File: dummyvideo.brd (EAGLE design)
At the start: 26.3 x 27.9 mm, 12 parts, among them IC1 NE555

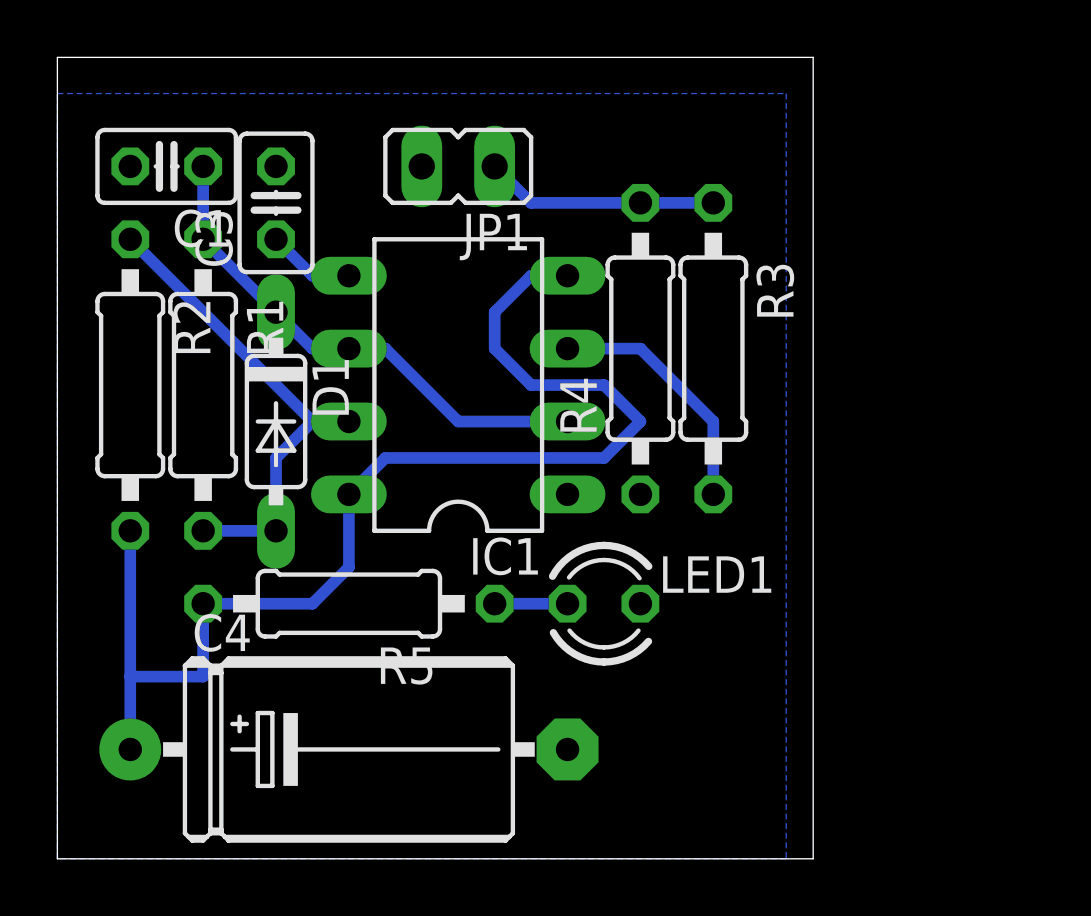
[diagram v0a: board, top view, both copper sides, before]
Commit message: Added power and mount holes.
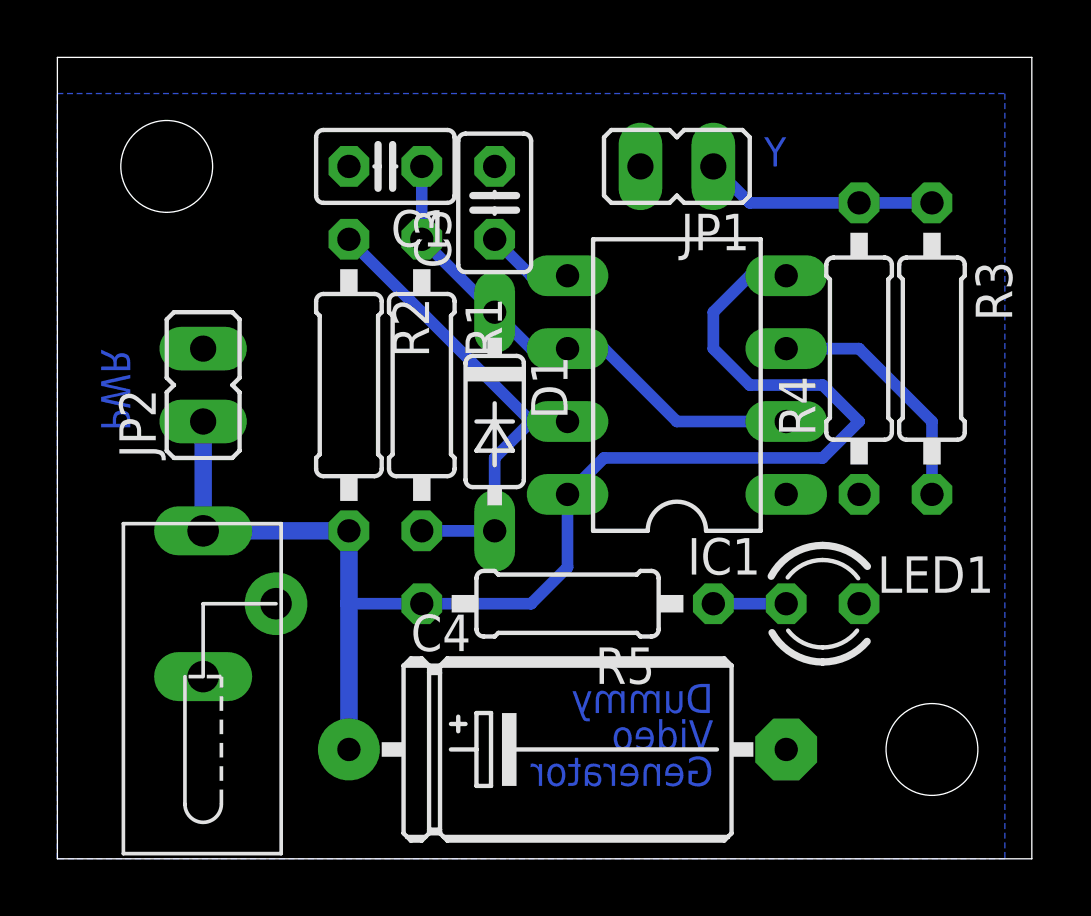
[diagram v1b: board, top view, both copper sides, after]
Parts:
- added JP2: POWER, jumper:JP1
- added U$1: DC_JACK, n39:DC_JACK_HEBO13
- JP1: value (none) -> Y
- moved C4 7.62 mm to (17.8, 3.81)
- moved LED1 7.62 mm to (26.7, 8.89)
- moved R3 7.62 mm to (30.5, 17.8)
- moved R4 7.62 mm to (27.9, 17.8)
- moved R5 7.62 mm to (17.8, 8.89)
- moved C3 7.62 mm to (15.2, 22.9)
- moved D1 7.62 mm to (15.2, 15.2)
- moved R2 7.62 mm to (10.2, 16.5)
- moved C1 7.62 mm to (11.4, 24.1)
- moved IC1 7.62 mm to (21.6, 16.5)
- moved JP1 7.62 mm to (21.6, 24.1)
- moved R1 7.62 mm to (12.7, 16.5)
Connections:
- net GND: now also JP2.2, U$1.OUTER
- net VCC: now also JP2.1, U$1.INNER
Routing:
- net VCC: track 42.5 -> 48.9 mm
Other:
- board size 26.3 x 27.9 mm -> 34 x 27.9 mm
- board text added: "Dummy"
- board text added: "Generator"
- board text added: "PWR"
- board text added: "Video"
- board text added: "Y"

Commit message: Wiederstand vor der LED angepasst
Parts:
- R5: value 220R -> 330R
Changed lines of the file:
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@@
 <element name="R4" library="resistor" package="0207/10" value="1,5K" x="27.94" y="17.78" rot="R90"/>
 <element name="LED1" library="led" package="LED3MM" value="bl" x="26.67" y="8.89"/>
-<element name="R5" library="resistor" package="0207/10" value="220R" x="17.78" y="8.89" rot="R180"/>
+<element name="R5" library="resistor" package="0207/10" value="330R" x="17.78" y="8.89" rot="R180"/>
 <element name="JP1" library="jumper" package="JP1" value="Y" x="21.59" y="24.13" rot="R90"/>
 <element name="U$1" library="n39" package="DC_JACK_HEBO13" value="DC_JACK" x="5.08" y="10.16"/>

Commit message: First revision of SMD board
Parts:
- removed JP1: Y, jumper:JP1
- removed JP2: POWER, jumper:JP1
- removed U$1: DC_JACK, n39:DC_JACK_HEBO13
- added JP_PAD1, JP_PAD2, PAD_Y, PWR_PAD_GND, PWR_PAD_VCC: (no value), wirepad:SMD1,27-2,54
- C1, C3: device resistor:C025-025X050 -> resistor:C0805
- C4: value 100u -> 47u; device resistor:E15-6 -> resistor:153CLV-0505
- IC1: value NE555 -> NE555SO; device st-microelectronics:DIL-08 -> n39:SO08
- LED1: value bl -> gn LC; device led:LED3MM -> led:CHIPLED-0603-TTW
- R1, R3, R4: device resistor:0207/10 -> resistor:R0805
- R2: device resistor:0207/10 -> resistor:M0805
- R5: value 330R -> 1,5K; device resistor:0207/10 -> resistor:R0805
- moved LED1 70.1 mm to (-33.0, 45.7)
- moved R4 63.5 mm to (-31.8, 39.4), turned to 0 degrees
- moved R3 54.0 mm to (-19.1, 39.4), turned to 0 degrees
- moved R5 51.2 mm to (-19.1, 44.5), turned to 0 degrees
- moved C1 48.4 mm to (-36.8, 20.3), turned to 0 degrees
- moved D1 46.6 mm to (-29.2, 29.2), turned to 0 degrees
- moved R2 45.5 mm to (-31.8, 34.3), turned to 0 degrees
- moved C4 42.7 mm to (-21.6, 20.3)
- moved R1 36.4 mm to (-19.1, 34.3), turned to 0 degrees
- moved C3 31.1 mm to (-15.2, 29.2), turned to 0 degrees
- moved IC1 13.0 mm to (8.89, 19.1), turned to 0 degrees
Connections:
- new net N$6: JP_PAD2.1, PWR_PAD_VCC.1
- net GND: now also LED1.C@1, PWR_PAD_GND.1; no longer JP1.2, JP2.2, LED1.K, U$1.OUTER
- net N$5: now also LED1.A@1; no longer LED1.A
- net OUT: now also PAD_Y.1; no longer JP1.1
- net VCC: now also JP_PAD1.1; no longer JP2.1, U$1.INNER
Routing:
- net VCC: track 48.9 -> 0.00 mm
- net N$3: track 17.9 -> 0.00 mm
- net N$1: track 17.1 -> 0.00 mm
- net N$4: track 8.67 -> 0.00 mm
- net OUT: track 8.15 -> 0.00 mm
- net N$2: track 3.07 -> 0.00 mm
- net N$5: track 2.54 -> 0.00 mm
- removed copper zone on layer 16, net GND
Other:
- board size 34 x 27.9 mm -> 20.3 x 33 mm
- board text removed: "Dummy"
- board text removed: "Generator"
- board text removed: "PWR"
- board text removed: "Video"
- board text removed: "Y"

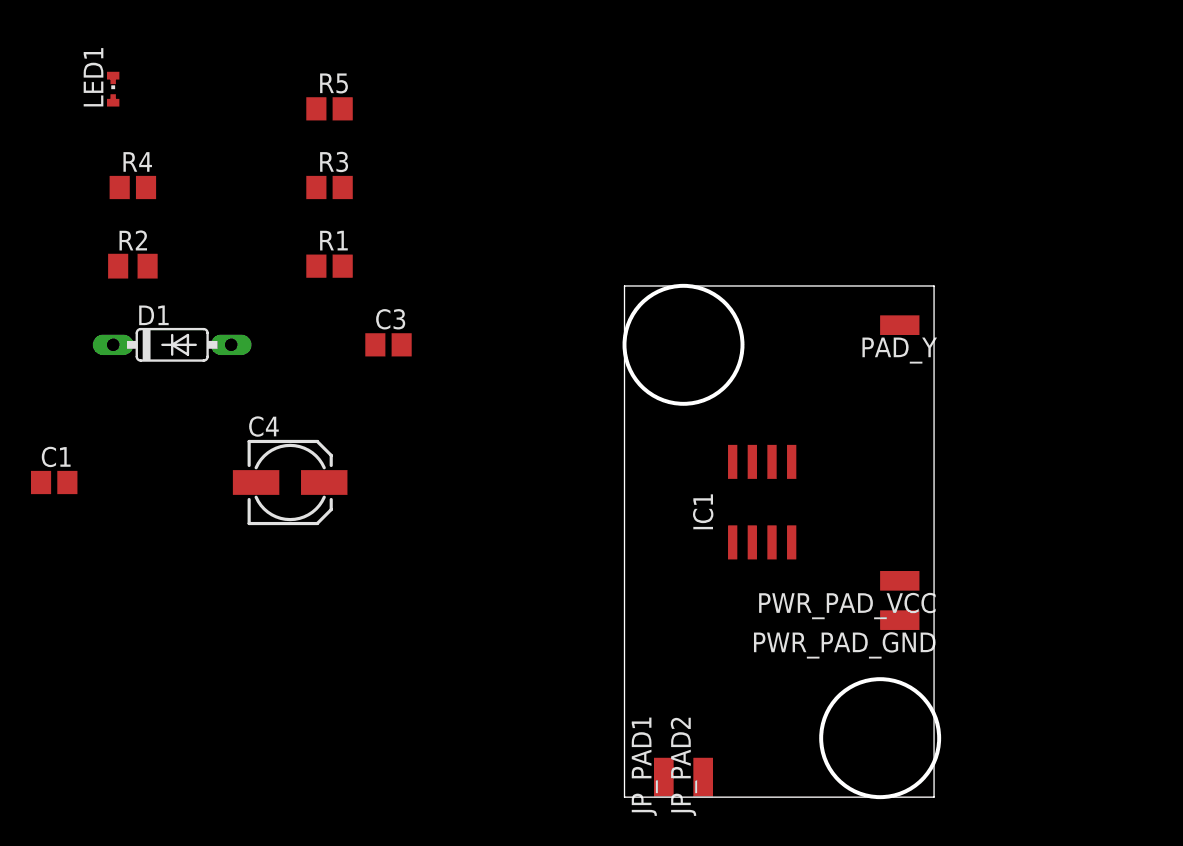
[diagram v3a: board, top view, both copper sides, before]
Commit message: Changed layout to SMD variant.
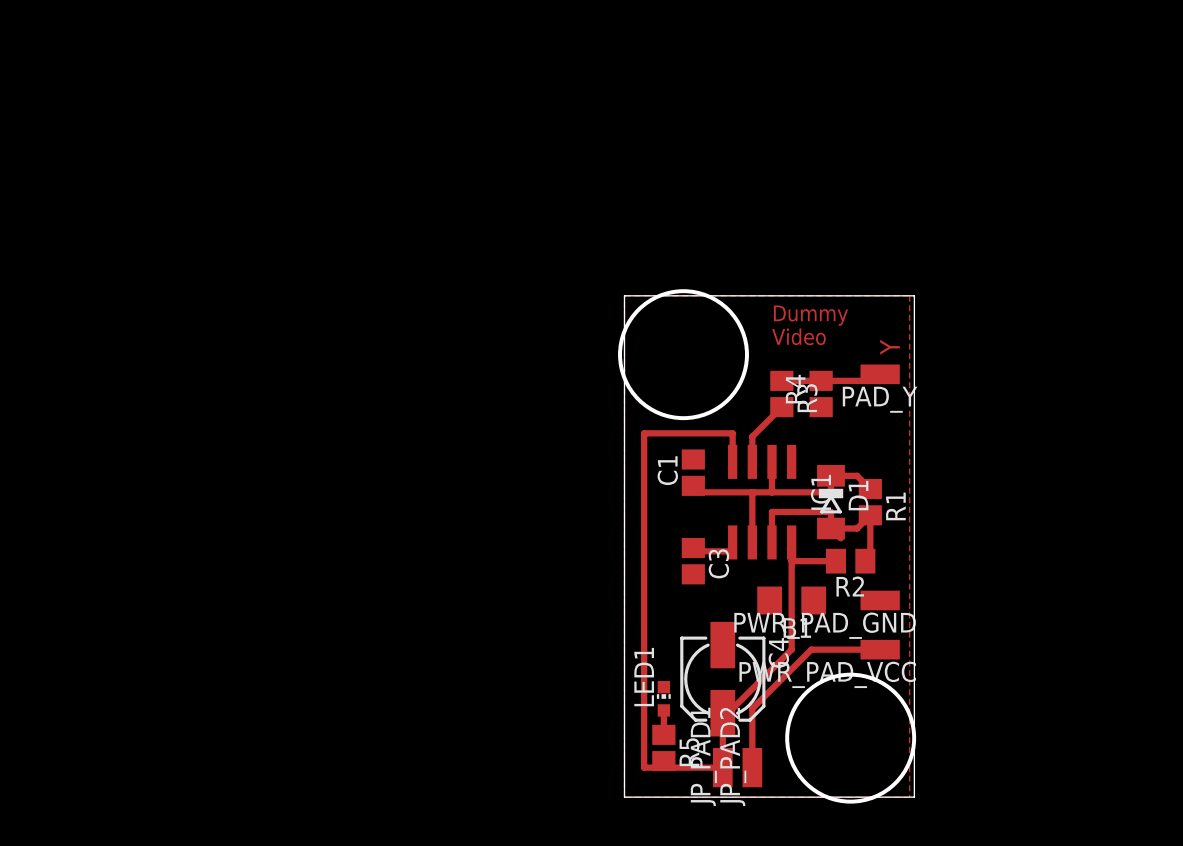
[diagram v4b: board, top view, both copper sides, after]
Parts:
- added B1: 000, resistor:R1206
- D1: value 1N4148DO35-7 -> 1N4148SOD-80; device diode:DO35-7 -> n39:SOD80C
- LED1: device led:CHIPLED-0603-TTW -> led:CHIP-LED0603
- moved LED1 53.1 mm to (2.54, 6.35)
- moved R2 50.1 mm to (14.6, 15.2), turned to 180 degrees
- moved R5 46.6 mm to (2.54, 3.17), turned to 270 degrees
- moved R4 46.4 mm to (12.7, 26.0), turned to 90 degrees
- moved D1 43.7 mm to (13.3, 19.1), turned to 270 degrees
- moved C1 41.3 mm to (4.45, 21.0), turned to 90 degrees
- moved R1 38.1 mm to (15.9, 19.1), turned to 270 degrees
- moved R3 32.1 mm to (10.2, 26.0), turned to 270 degrees
- moved C4 30.7 mm to (6.35, 7.62), turned to 270 degrees
- moved C3 24.1 mm to (4.45, 15.2), turned to 270 degrees
- moved PWR_PAD_VCC 4.62 mm to (16.5, 9.53)
- moved JP_PAD1 3.86 mm to (6.35, 1.91)
- moved PAD_Y 3.42 mm to (16.5, 27.3)
- moved JP_PAD2 3.24 mm to (8.26, 1.91)
- moved PWR_PAD_GND 1.80 mm to (16.5, 12.7)
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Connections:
- removed net N$6: JP_PAD2.1, PWR_PAD_VCC.1
- new net VCC_SW: C4.+, IC1.4, IC1.8, JP_PAD1.1, R2.2, R5.2
- net GND: now also B1.1, B1.2, LED1.C; no longer LED1.C@1
- net N$5: now also LED1.A; no longer LED1.A@1
- net VCC: now also JP_PAD2.1, PWR_PAD_VCC.1; no longer C4.+, IC1.4, IC1.8, JP_PAD1.1, R2.2, R5.2
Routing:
- net VCC_SW: track 0.00 -> 53.8 mm
- net N$3: track 0.00 -> 18.2 mm
- net N$1: track 0.00 -> 13.7 mm
- net VCC: track 0.00 -> 13.6 mm
- net OUT: track 0.00 -> 7.04 mm
- net N$4: track 0.00 -> 4.32 mm
- net N$2: track 0.00 -> 3.20 mm
- net N$5: track 0.00 -> 1.57 mm
- added copper zone on layer 1, net GND
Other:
- board size 20.3 x 33 mm -> 19 x 33 mm
- board text added: "Dummy Video"
- board text added: "Y"
